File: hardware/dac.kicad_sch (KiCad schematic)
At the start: 52 parts, among them SW3 SW_DIP_x03, SW4 SW_DIP_x03, SW5 SW_DIP_x03, SW6 SW_DIP_x03, U28 REF5030ID, U31 MCP4728, U33 MCP4728, U34 MCP4728, U35 MCP4728, U36 MCP4728, U37 MCP4728, U38 REF5050ID, U39 REF5030ID, U40 REF5050ID

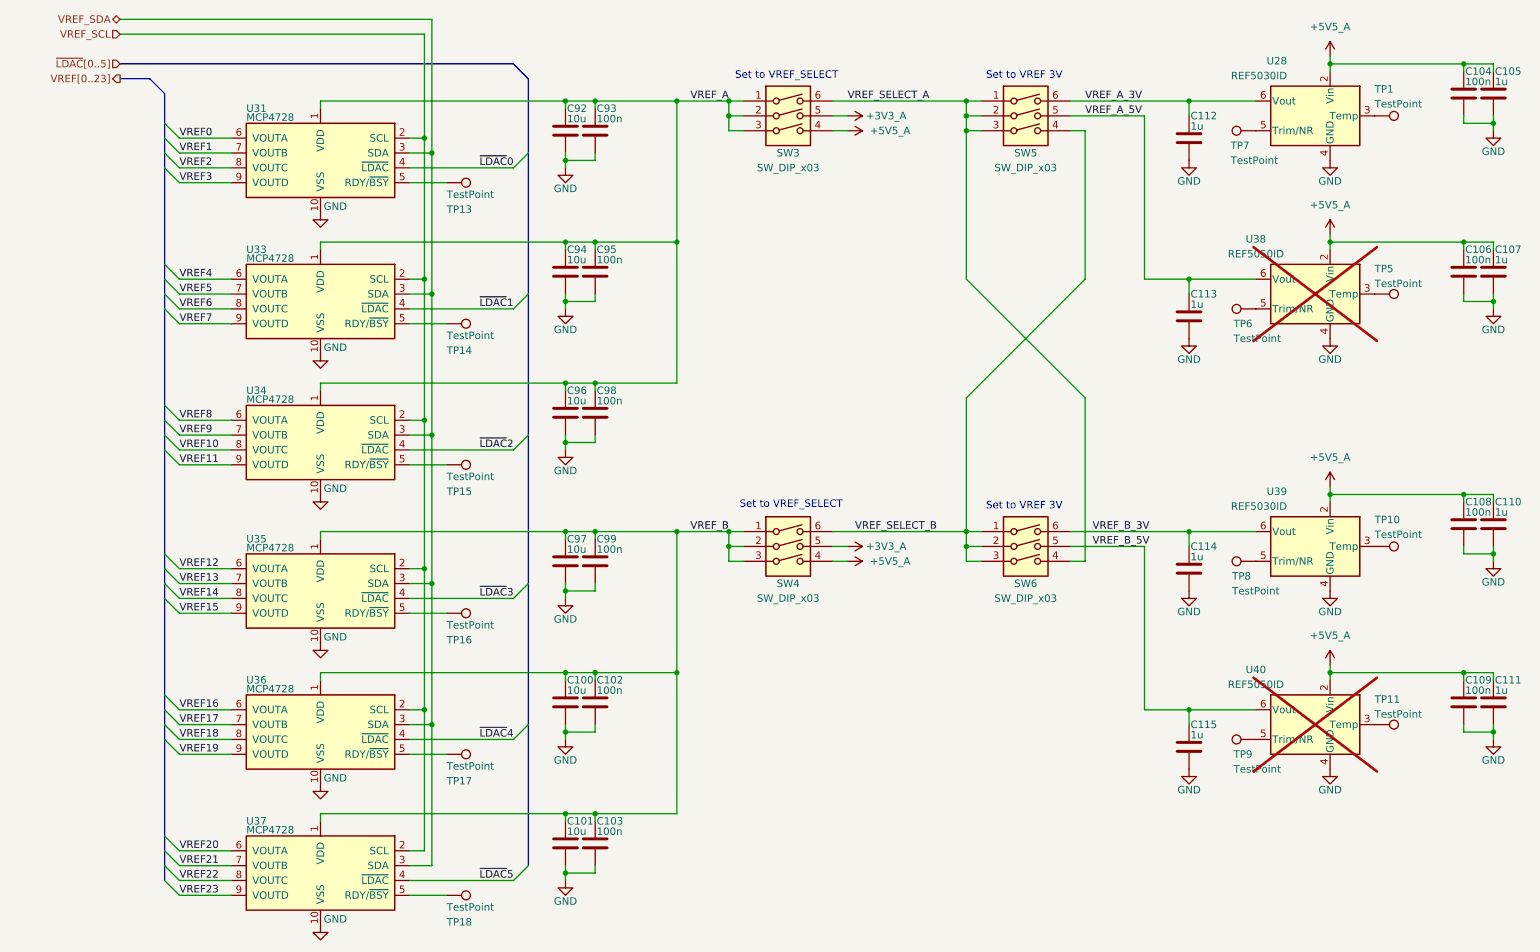
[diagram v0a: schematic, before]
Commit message: complete schematic wiring
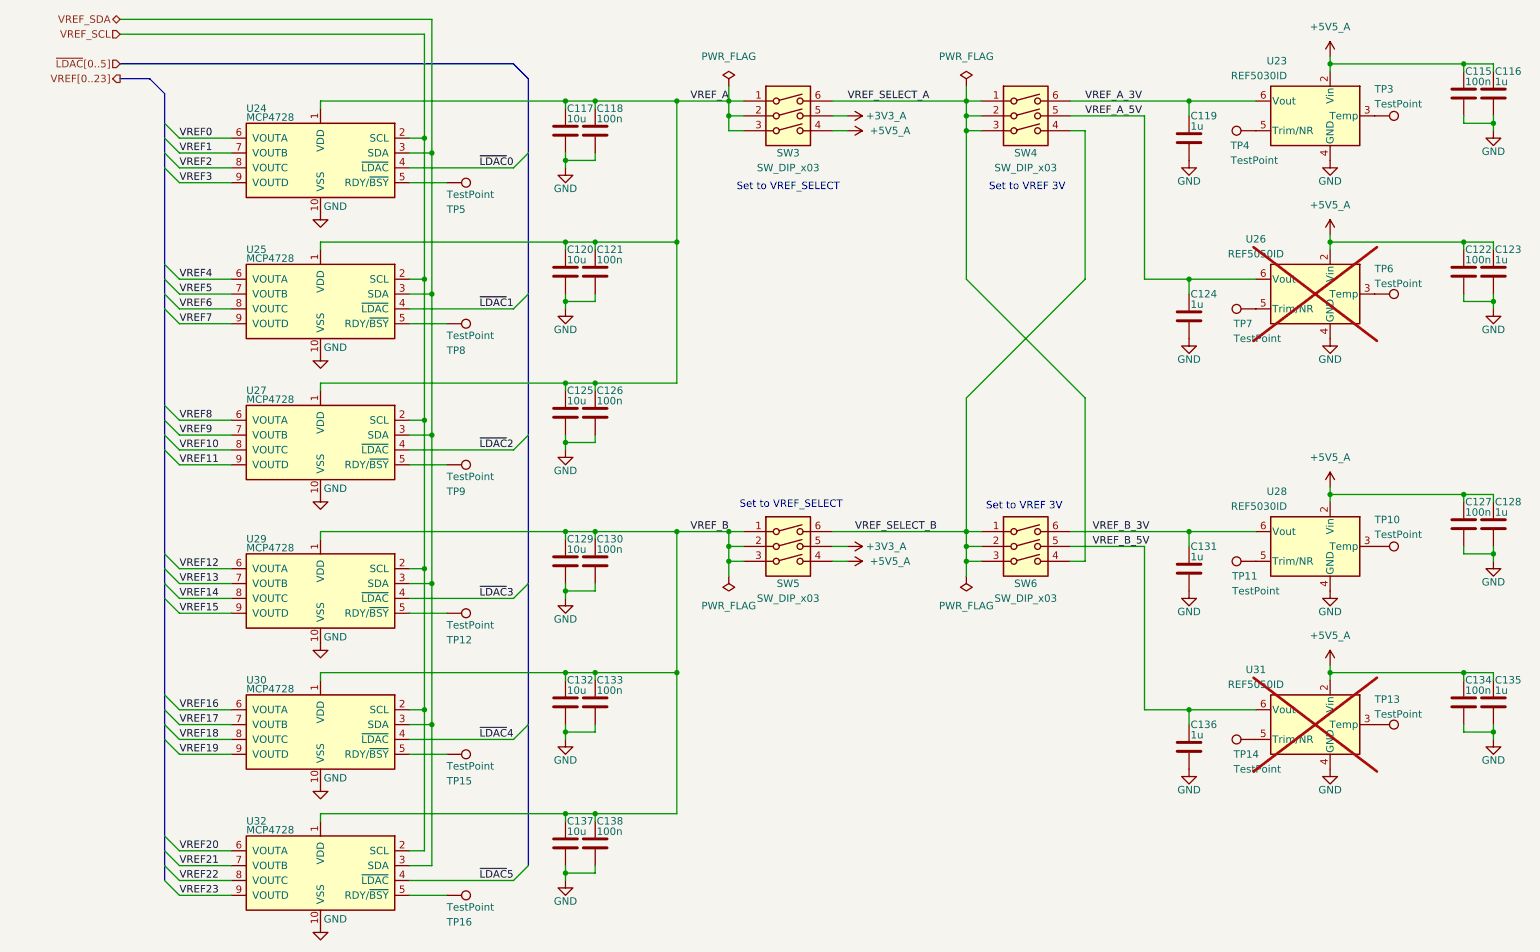
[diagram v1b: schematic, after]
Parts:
- renumbered C104 to C115, C105 to C116, C92 to C117, C93 to C118, C112 to C119, C94 to C120, C95 to C121, C106 to C122, C107 to C123, C113 to C124, C96 to C125, C98 to C126, C108 to C127, C110 to C128, C97 to C129, C99 to C130, C114 to C131, C100 to C132, C102 to C133, C109 to C134, C111 to C135, C115 to C136, C101 to C137, C103 to C138, SW5 to SW4, SW4 to SW5, TP8 to TP11, TP16 to TP12, TP11 to TP13, TP9 to TP14, TP17 to TP15, TP18 to TP16, TP1 to TP3, TP7 to TP4, TP13 to TP5, TP5 to TP6, TP6 to TP7, TP14 to TP8, TP15 to TP9, U28 to U23, U31 to U24, U33 to U25, U38 to U26, U34 to U27, U39 to U28, U35 to U29, U36 to U30, U40 to U31, U37 to U32

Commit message: update power system + add LCSC part numbers
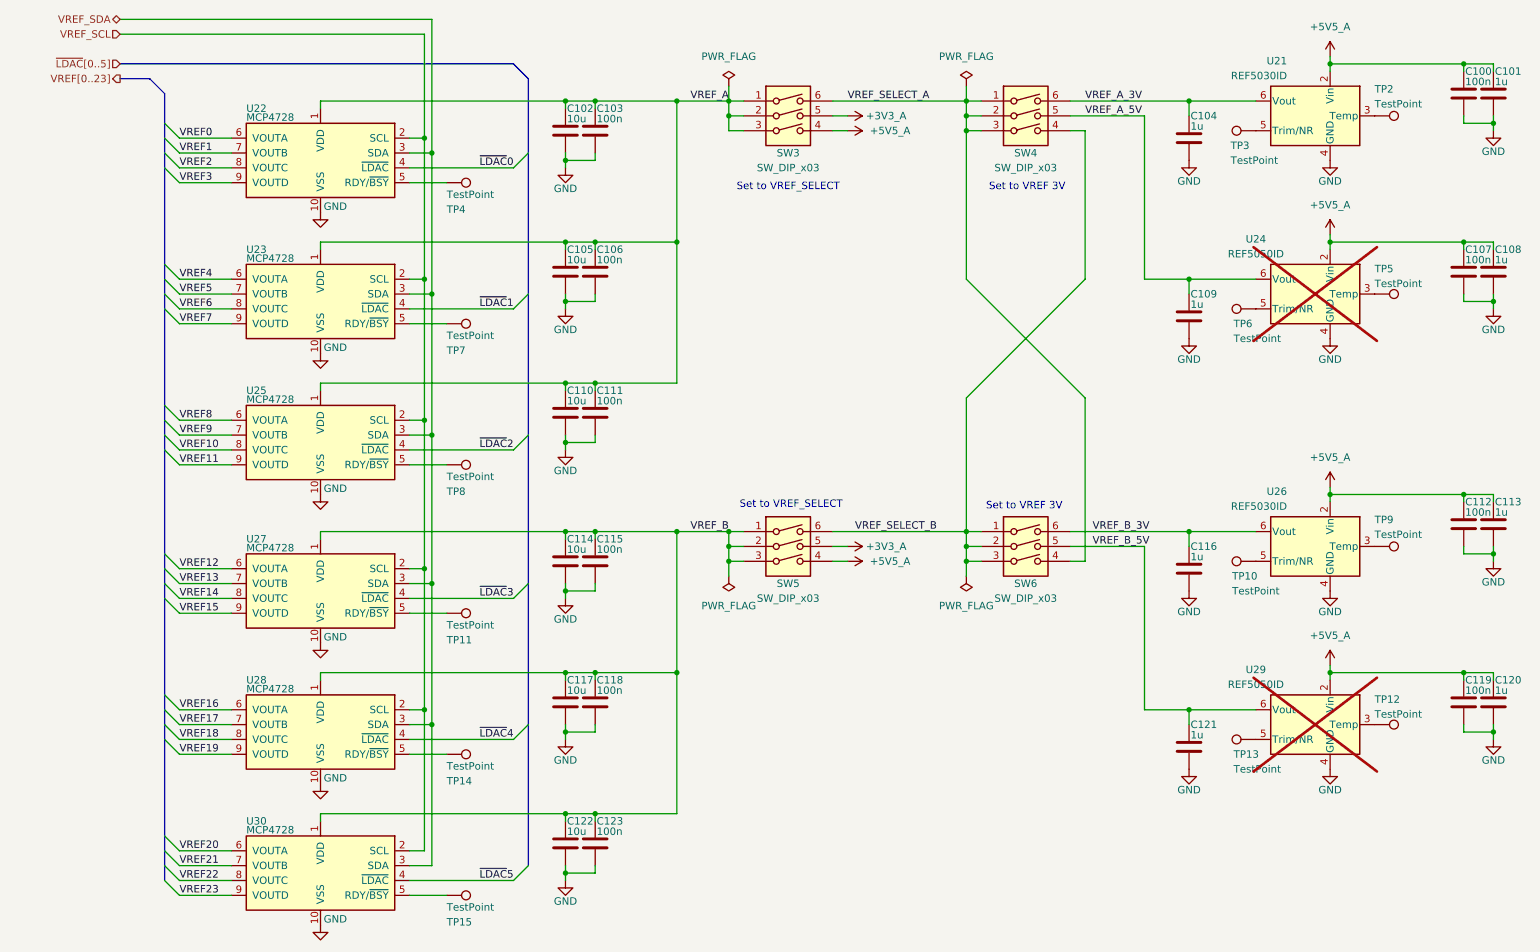
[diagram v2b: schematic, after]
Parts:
- C100: renamed from C115; footprint (none) -> Capacitor_SMD:C_0402_1005Metric; LCSC (none) -> C307331
- C101: renamed from C116; footprint (none) -> Capacitor_SMD:C_0805_2012Metric; LCSC (none) -> C28323
- C102: renamed from C117; footprint (none) -> Capacitor_SMD:C_1206_3216Metric; LCSC (none) -> C13585
- C103: renamed from C118; footprint (none) -> Capacitor_SMD:C_0402_1005Metric; LCSC (none) -> C307331
- C104: renamed from C119; footprint (none) -> Capacitor_SMD:C_0805_2012Metric; LCSC (none) -> C28323
- C105: renamed from C120; footprint (none) -> Capacitor_SMD:C_1206_3216Metric; LCSC (none) -> C13585
- C106: renamed from C121; footprint (none) -> Capacitor_SMD:C_0402_1005Metric; LCSC (none) -> C307331
- C107: renamed from C122; footprint (none) -> Capacitor_SMD:C_0402_1005Metric; LCSC (none) -> C307331
- C108: renamed from C123; footprint (none) -> Capacitor_SMD:C_0805_2012Metric; LCSC (none) -> C28323
- C109: renamed from C124; footprint (none) -> Capacitor_SMD:C_0805_2012Metric; LCSC (none) -> C28323
- C110: renamed from C125; footprint (none) -> Capacitor_SMD:C_1206_3216Metric; LCSC (none) -> C13585
- C111: renamed from C126; footprint (none) -> Capacitor_SMD:C_0402_1005Metric; LCSC (none) -> C307331
- C112: renamed from C127; footprint (none) -> Capacitor_SMD:C_0402_1005Metric; LCSC (none) -> C307331
- C113: renamed from C128; footprint (none) -> Capacitor_SMD:C_0805_2012Metric; LCSC (none) -> C28323
- C114: renamed from C129; footprint (none) -> Capacitor_SMD:C_1206_3216Metric; LCSC (none) -> C13585
- C115: renamed from C130; footprint (none) -> Capacitor_SMD:C_0402_1005Metric; LCSC (none) -> C307331
- C116: renamed from C131; footprint (none) -> Capacitor_SMD:C_0805_2012Metric; LCSC (none) -> C28323
- C117: renamed from C132; footprint (none) -> Capacitor_SMD:C_1206_3216Metric; LCSC (none) -> C13585
- C118: renamed from C133; footprint (none) -> Capacitor_SMD:C_0402_1005Metric; LCSC (none) -> C307331
- C119: renamed from C134; footprint (none) -> Capacitor_SMD:C_0402_1005Metric; LCSC (none) -> C307331
- C120: renamed from C135; footprint (none) -> Capacitor_SMD:C_0805_2012Metric; LCSC (none) -> C28323
- C121: renamed from C136; footprint (none) -> Capacitor_SMD:C_0805_2012Metric; LCSC (none) -> C28323
- C122: renamed from C137; footprint (none) -> Capacitor_SMD:C_1206_3216Metric; LCSC (none) -> C13585
- C123: renamed from C138; footprint (none) -> Capacitor_SMD:C_0402_1005Metric; LCSC (none) -> C307331
- SW3, SW4, SW5, SW6: footprint (none) -> Button_Switch_SMD:SW_DIP_SPSTx03_Slide_6.7x9.18mm_W8.61mm_P2.54mm_LowProfile; LCSC (none) -> C129079
- TP10: renamed from TP11; footprint (none) -> TestPoint:TestPoint_Pad_D1.0mm
- TP11: renamed from TP12; footprint (none) -> TestPoint:TestPoint_Pad_D1.0mm
- TP12: renamed from TP13; footprint (none) -> TestPoint:TestPoint_Pad_D1.0mm
- TP13: renamed from TP14; footprint (none) -> TestPoint:TestPoint_Pad_D1.0mm
- TP14: renamed from TP15; footprint (none) -> TestPoint:TestPoint_Pad_D1.0mm
- TP15: renamed from TP16; footprint (none) -> TestPoint:TestPoint_Pad_D1.0mm
- TP2: renamed from TP3; footprint (none) -> TestPoint:TestPoint_Pad_D1.0mm
- TP3: renamed from TP4; footprint (none) -> TestPoint:TestPoint_Pad_D1.0mm
- TP4: renamed from TP5; footprint (none) -> TestPoint:TestPoint_Pad_D1.0mm
- TP5: renamed from TP6; footprint (none) -> TestPoint:TestPoint_Pad_D1.0mm
- TP6: renamed from TP7; footprint (none) -> TestPoint:TestPoint_Pad_D1.0mm
- TP7: renamed from TP8; footprint (none) -> TestPoint:TestPoint_Pad_D1.0mm
- TP8: renamed from TP9; footprint (none) -> TestPoint:TestPoint_Pad_D1.0mm
- TP9: renamed from TP10; footprint (none) -> TestPoint:TestPoint_Pad_D1.0mm
- U21: renamed from U23; LCSC (none) -> C2878155
- U22: renamed from U24; LCSC (none) -> C108207
- U23: renamed from U25; LCSC (none) -> C108207
- U25: renamed from U27; LCSC (none) -> C108207
- U26: renamed from U28; LCSC (none) -> C2878155
- U27: renamed from U29; LCSC (none) -> C108207
- U28: renamed from U30; LCSC (none) -> C108207
- U30: renamed from U32; LCSC (none) -> C108207
- renumbered U26 to U24, U31 to U29

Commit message: apply manufacturing BOM
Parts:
- renumbered C100 to C104, C101 to C105, C102 to C106, C103 to C107, C104 to C108, C105 to C109, C106 to C110, C107 to C111, C108 to C112, C109 to C113, C110 to C114, C111 to C115, C112 to C116, C113 to C117, C114 to C118, C115 to C119, C116 to C120, C117 to C121, C118 to C122, C119 to C123, C120 to C124, C121 to C125, C122 to C126, C123 to C127

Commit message: route more
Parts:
- added TP16, TP18, TP19, TP20, TP21, TP22, TP23, TP24, TP25, TP26, TP27, TP28, TP29, TP30, TP31, TP32, TP33, TP34, TP35, TP36, TP37, TP38, TP39, TP40, TP41, TP42: TestPoint_Alt, digital:TestPoint_Keystone_5015_Micro_Mini, symbol Connector:TestPoint_Alt
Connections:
- net VREF0: now also TP19.1
- net VREF1: now also TP20.1
- net VREF10: now also TP29.1
- net VREF11: now also TP30.1
- net VREF12: now also TP31.1
- net VREF13: now also TP32.1
- net VREF14: now also TP33.1
- net VREF15: now also TP34.1
- net VREF16: now also TP35.1
- net VREF17: now also TP36.1
- net VREF18: now also TP37.1
- net VREF19: now also TP38.1
- net VREF2: now also TP21.1
- net VREF20: now also TP39.1
- net VREF21: now also TP40.1
- net VREF22: now also TP41.1
- net VREF23: now also TP42.1
- net VREF3: now also TP22.1
- net VREF4: now also TP23.1
- net VREF5: now also TP24.1
- net VREF6: now also TP25.1
- net VREF7: now also TP26.1
- net VREF8: now also TP27.1
- net VREF9: now also TP28.1
- net VREF_A: now also TP18.1
- net VREF_B: now also TP16.1

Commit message: route
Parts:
- renumbered C104 to C74, C105 to C75, C106 to C76, C107 to C77, C108 to C78, C109 to C79, C110 to C80, C111 to C81, C112 to C82, C113 to C83, C114 to C84, C115 to C85, C116 to C86, C117 to C87, C118 to C88, C119 to C89, C120 to C90, C121 to C91, C122 to C92, C123 to C93, C124 to C94, C125 to C95, C126 to C96, C127 to C97, SW3 to SW2, SW4 to SW3, SW5 to SW4, SW6 to SW5, TP22 to TP10, TP4 to TP11, TP23 to TP12, TP24 to TP13, TP5 to TP14, TP25 to TP15, TP6 to TP16, TP26 to TP17, TP7 to TP18, TP27 to TP19, TP28 to TP20, TP29 to TP21, TP30 to TP22, TP8 to TP23, TP16 to TP24, TP9 to TP25, TP31 to TP26, TP10 to TP27, TP32 to TP28, TP33 to TP29, TP34 to TP30, TP11 to TP31, TP35 to TP32, TP36 to TP33, TP12 to TP34, TP37 to TP35, TP13 to TP36, TP38 to TP37, TP14 to TP38, TP18 to TP4, TP15 to TP43, TP2 to TP5, TP3 to TP6, TP19 to TP7, TP20 to TP8, TP21 to TP9, U21 to U14, U22 to U15, U23 to U16, U24 to U17, U25 to U18, U26 to U19, U27 to U20, U28 to U21, U29 to U22, U30 to U23
